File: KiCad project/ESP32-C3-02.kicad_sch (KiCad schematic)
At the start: 27 parts, among them J3 GSD090012SEU, U3 ESP32-C3-WROOM-02-H4, U4 CP2102N-A02-GQFN20, U5 USBLC6-2SC6, U6 W25Q32JVSSIQ

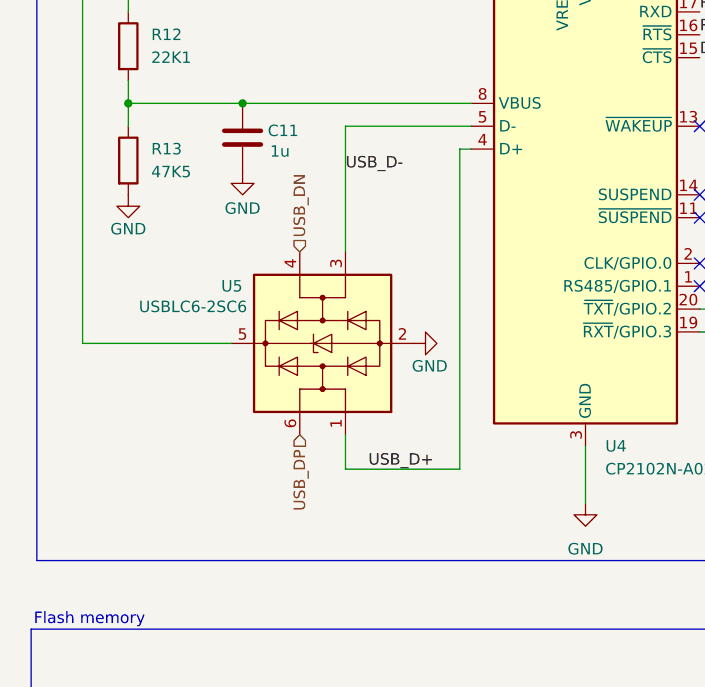
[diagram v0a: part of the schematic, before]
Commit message: Replaced USB C receptacle with a different model. Repositioning components to better align with manufacturer recommendations.
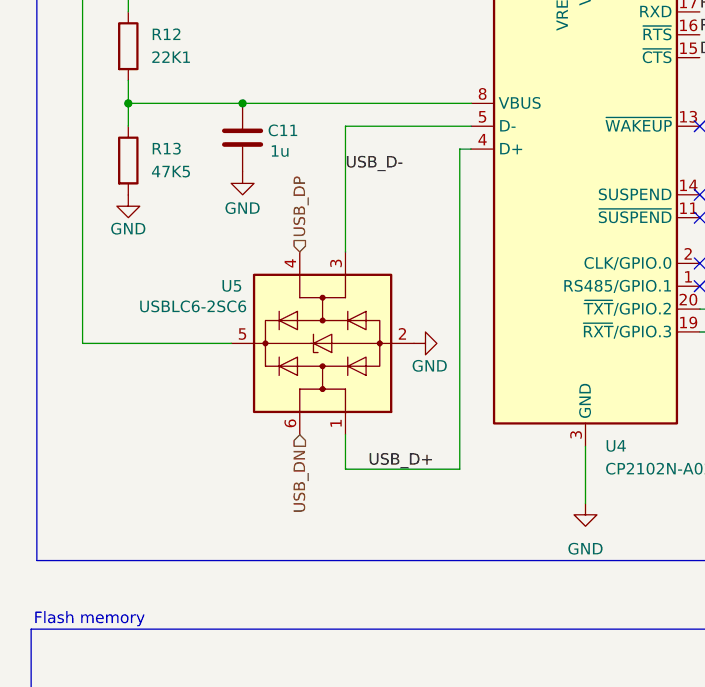
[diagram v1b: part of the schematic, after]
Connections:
- net USB_DN: now also U5.6 (I/O1); no longer U5.4 (I/O2)
- net USB_DP: now also U5.4 (I/O2); no longer U5.6 (I/O1)
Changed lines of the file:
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@@
 	(hierarchical_label "USB_DP"
+		(shape input)
+		(at 48.26 96.52 90)
+		(fields_autoplaced yes)
+		(effects
+			(font
+				(size 1.27 1.27)
+			)
+			(justify left)
+		)
+	)
+	(hierarchical_label "USB_DN"
 		(shape input)
 		(at 48.26 116.84 270)
@@
 		)
 	)
-	(hierarchical_label "USB_DN"
-		(shape input)
-		(at 48.26 96.52 90)
-		(fields_autoplaced yes)
-		(effects
-			(font
-				(size 1.27 1.27)
-			)
-			(justify left)
-		)
-	)

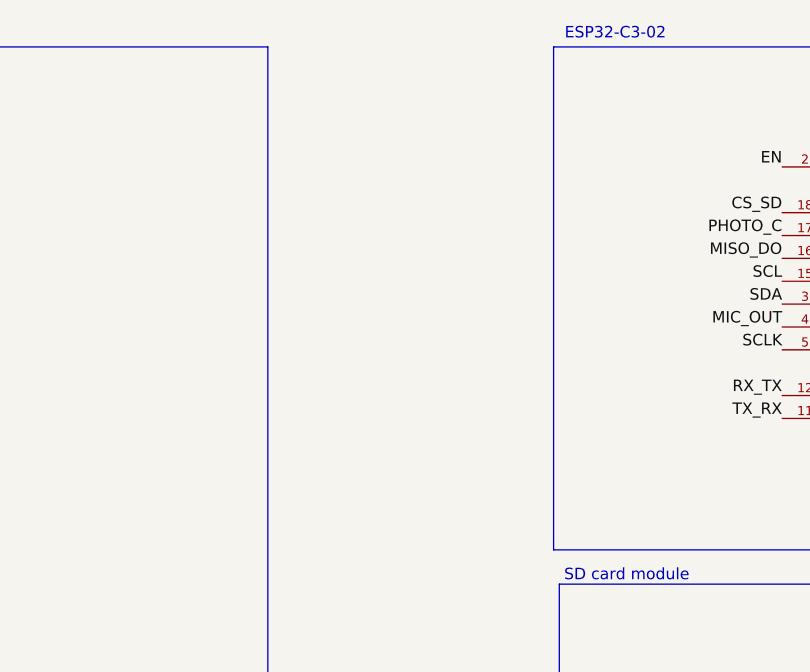
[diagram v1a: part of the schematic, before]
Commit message: Work in progress, new layout and routing.
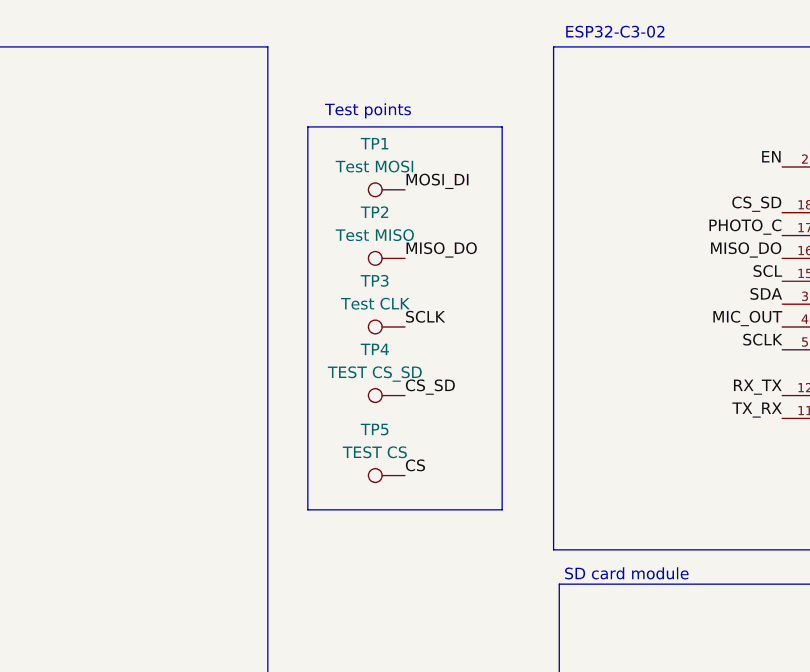
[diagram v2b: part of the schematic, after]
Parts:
- added TP1: Test MOSI, TestPoint:TestPoint_Pad_D1.0mm, symbol Connector:TestPoint
- added TP2: Test MISO, TestPoint:TestPoint_Pad_D1.0mm, symbol Connector:TestPoint
- added TP3: Test CLK, TestPoint:TestPoint_Pad_D1.0mm, symbol Connector:TestPoint
- added TP4: TEST CS_SD, TestPoint:TestPoint_Pad_D1.0mm, symbol Connector:TestPoint
- added TP5: TEST CS, TestPoint:TestPoint_Pad_D1.0mm, symbol Connector:TestPoint
- C12, C7, C9: footprint T491A -> Footprints:T491A
- D5, D6: footprint LEDC2012X120N -> Footprints:LEDC2012X120N
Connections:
- net CS: now also TP5.1
- net CS_SD: now also TP4.1
- net MISO_DO: now also TP2.1
- net MOSI_DI: now also TP1.1
- net SCLK: now also TP3.1
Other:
- note added: "Test points"

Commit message: Optimisation complete.
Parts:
- removed R17, R21: 50, Resistor_SMD:R_0805_2012Metric, symbol Device:R
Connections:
- net MOSI_DI: now also J3.2 (CMD), R15.1, U6.5 (DI(IO0)); no longer R15.2, U3.6 (IO7)
- net SCLK: now also J3.5 (CLK), U6.6 (CLK); no longer U3.5 (IO6)
- net USB_D+: now also U5.3 (I/O2); no longer U5.1 (I/O1)
- net USB_D-: now also U5.1 (I/O1); no longer U5.3 (I/O2)
- net at R20.2: now also U3.5 (IO6); no longer U6.6 (CLK)
- new net: R15.2, U3.6 (IO7)
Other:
- moved on the sheet: R15, R20

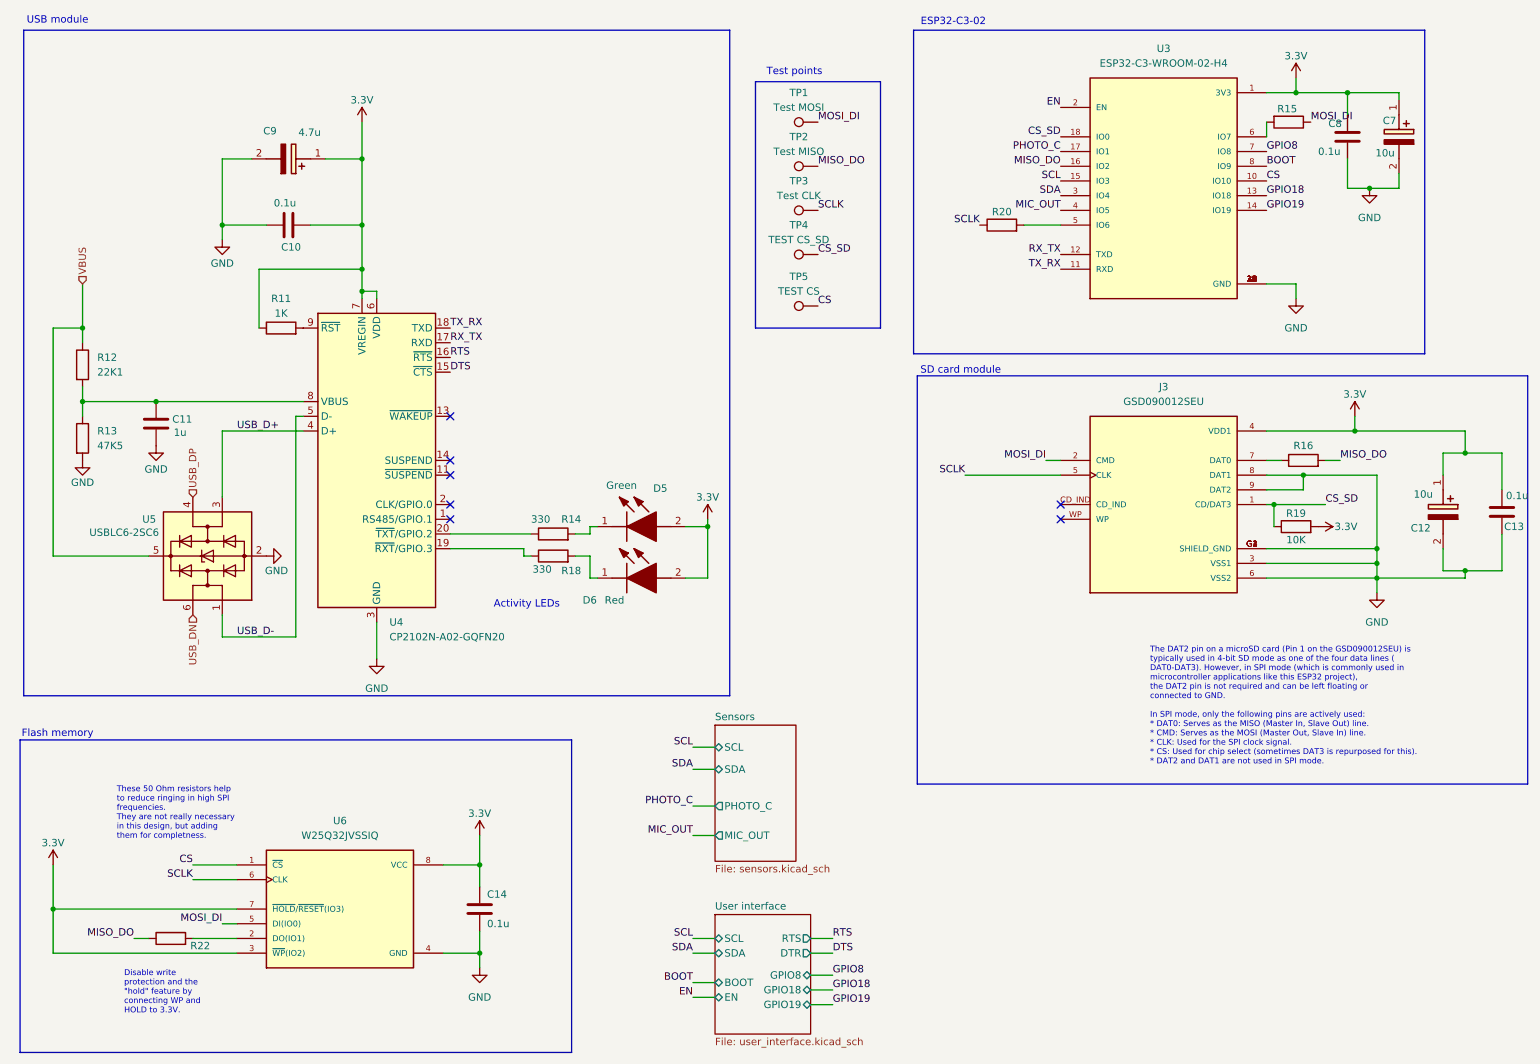
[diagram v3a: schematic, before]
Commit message: Fixed and improved Schematic design:
* Changed the buttons
* Added a ferrite bead at the output of the charger to cut some possible noise.
* Changed the values of R30, R31 and C19, and i add a 100K trimmer to set the gain from 25x to 125x.
* Added C23, C24 and C25 in the photo sensor circuit
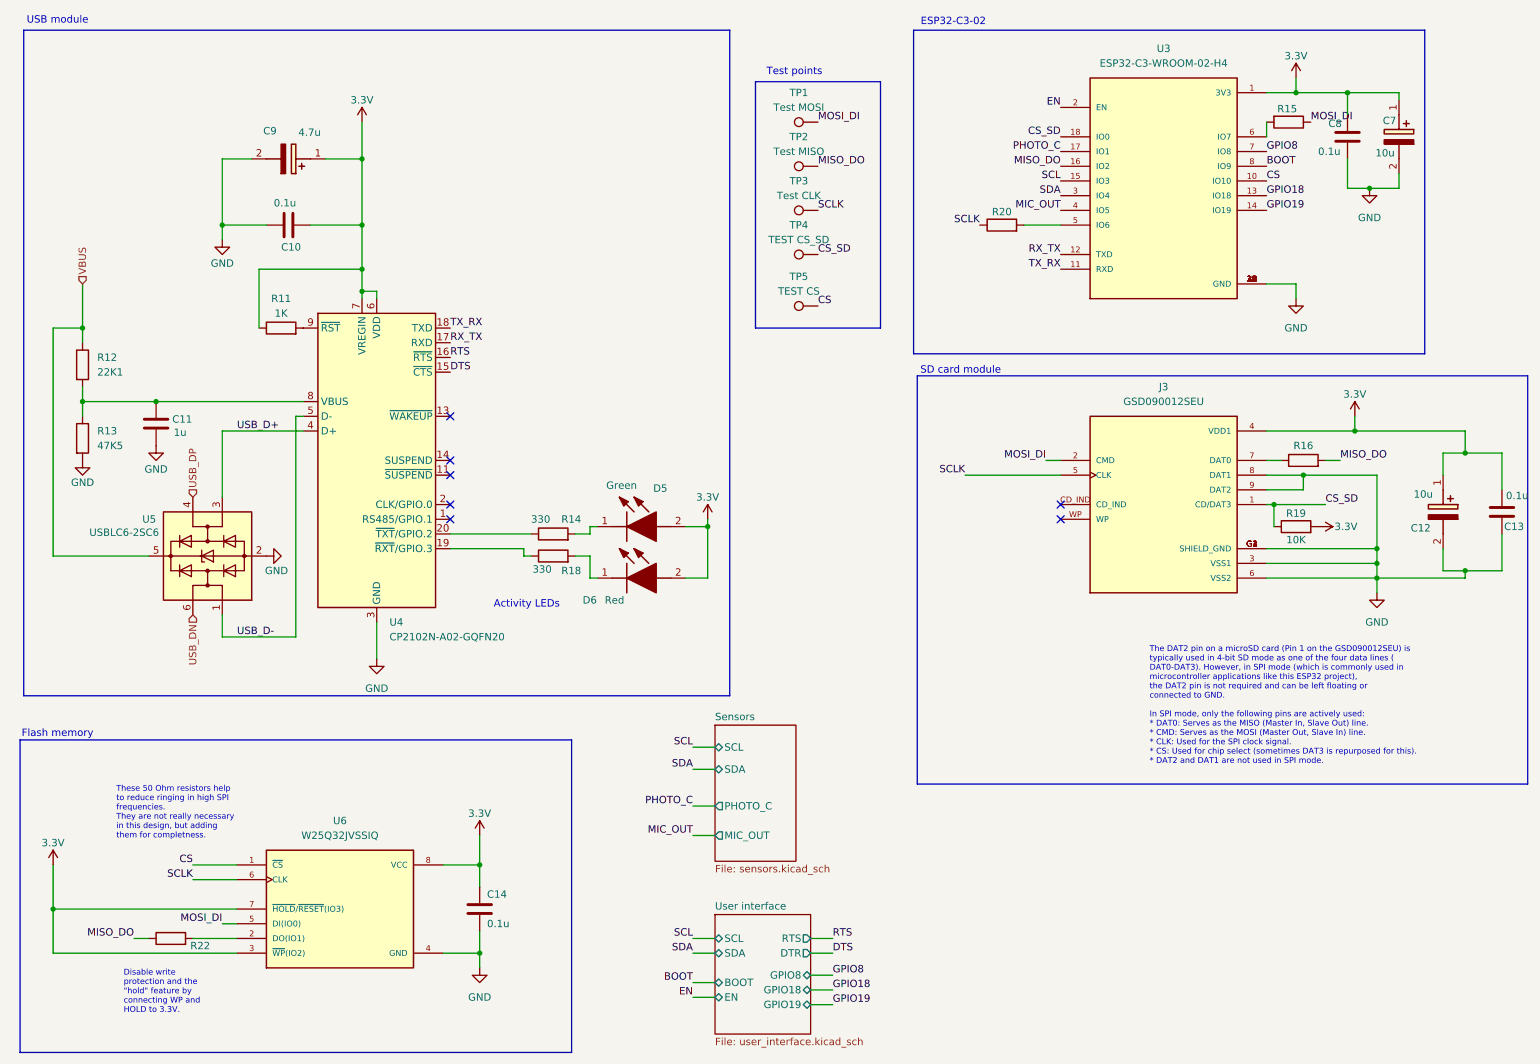
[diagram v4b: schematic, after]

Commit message: Completed schematic fixes and updates. Continuing with the layout for Prototype #2.
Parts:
- J3: footprint Project_Library:AMPHENOL_GSD090012SEU -> Footprints:AMPHENOL_GSD090012SEU
- U6: footprint Project_Library:SOIC127P790X216-8N -> Footprints:SOIC127P790X216-8N
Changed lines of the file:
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@@
 			)
 		)
-		(property "Footprint" "Project_Library:AMPHENOL_GSD090012SEU"
+		(property "Footprint" "Footprints:AMPHENOL_GSD090012SEU"
 			(at 215.9 97.79 0)
 			(effects
@@
 			)
 		)
-		(property "Footprint" "Project_Library:SOIC127P790X216-8N"
+		(property "Footprint" "Footprints:SOIC127P790X216-8N"
 			(at 73.66 167.64 0)
 			(effects

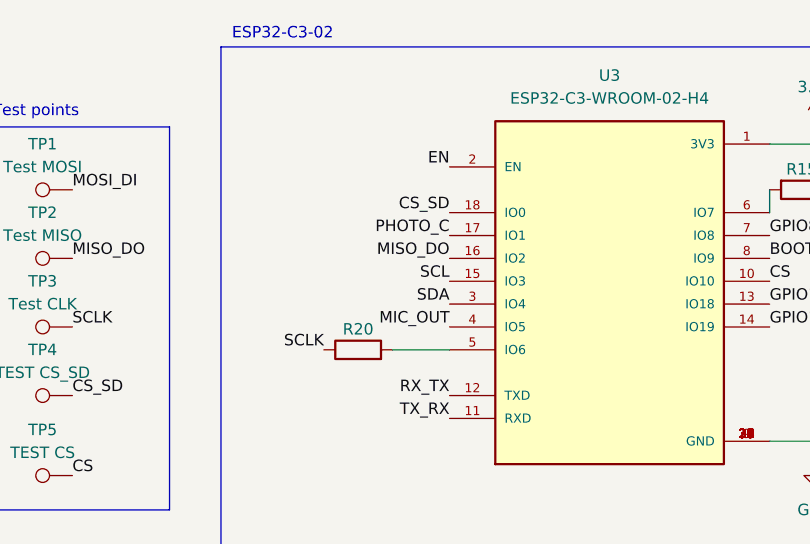
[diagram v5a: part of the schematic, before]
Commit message: Swapped pins for CS_SD and MIC_OUT so that the microphone is connected to a usable ADC.
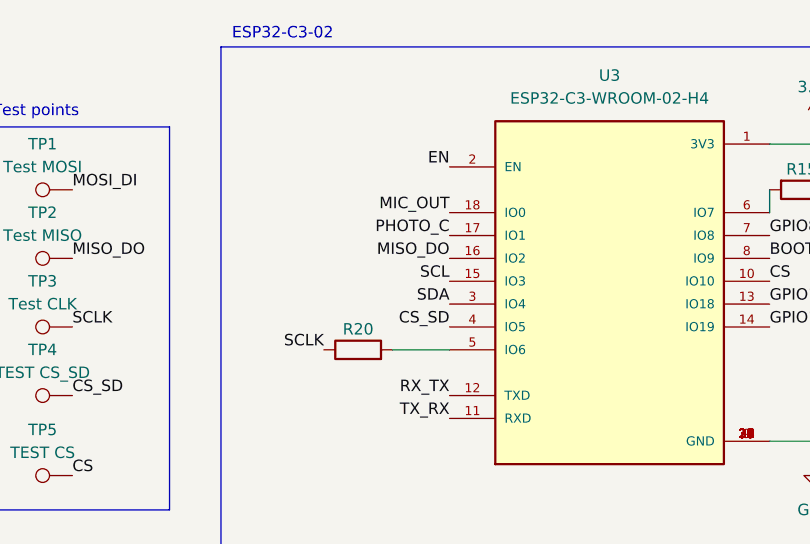
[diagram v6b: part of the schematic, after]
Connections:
- net CS_SD: now also U3.4 (IO5); no longer U3.18 (IO0)
- net MIC_OUT: now also U3.18 (IO0); no longer U3.4 (IO5)
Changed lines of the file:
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@@
 	)
 	(label "MIC_OUT"
-		(at 198.12 46.99 180)
+		(at 198.12 34.29 180)
 		(effects
 			(font
@@
 	)
 	(label "CS_SD"
-		(at 198.12 34.29 180)
+		(at 198.12 46.99 180)
 		(effects
 			(font
